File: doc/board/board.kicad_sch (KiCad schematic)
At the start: 11 parts, among them J1 Conn_01x02_Pin, SW2 RotaryEncoder_Switch_MP, U1 CR2013-MI2120, U2 PCM5102A, U3 INA219AxD

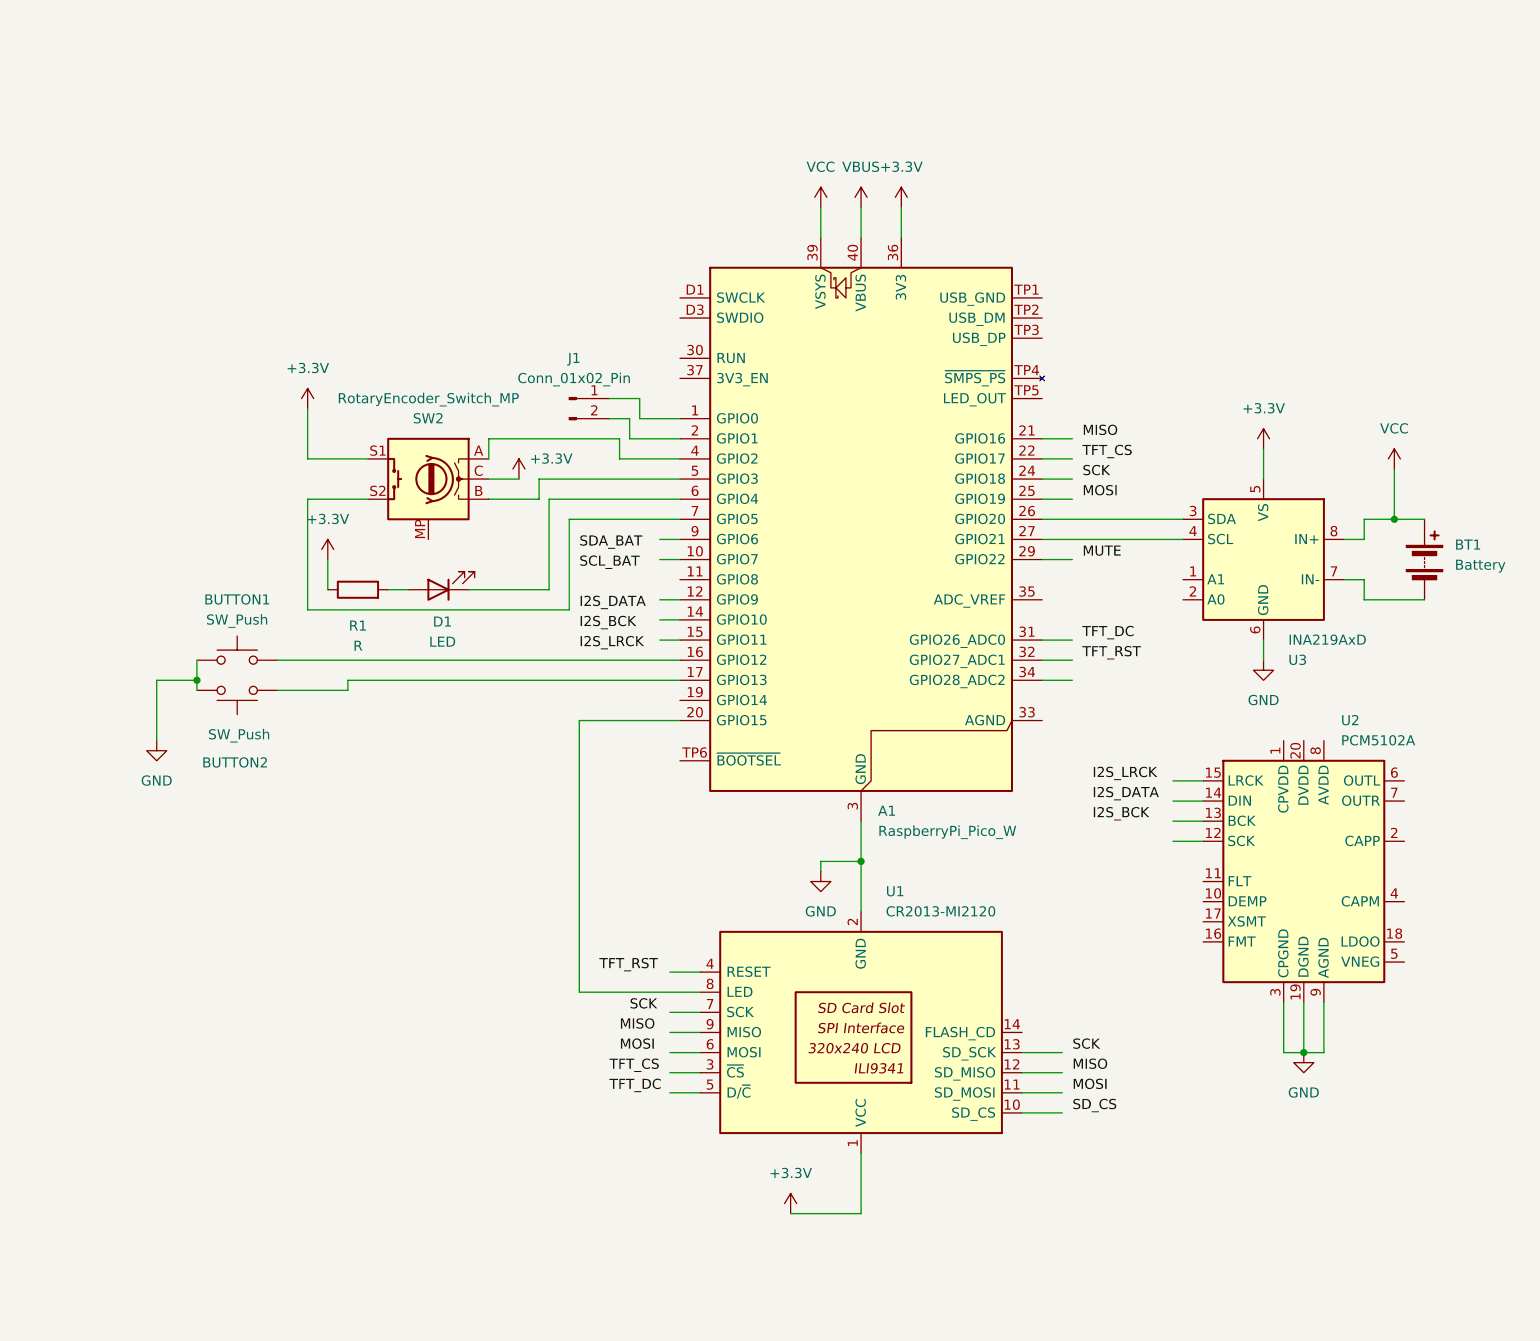
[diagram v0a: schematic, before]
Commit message: doc(datasheets, BoM, schematic)
- Update the schematic with the schmitt trigger
- Add the datasheets for the schmitt trigger
- Add the list of components to reproduce the board
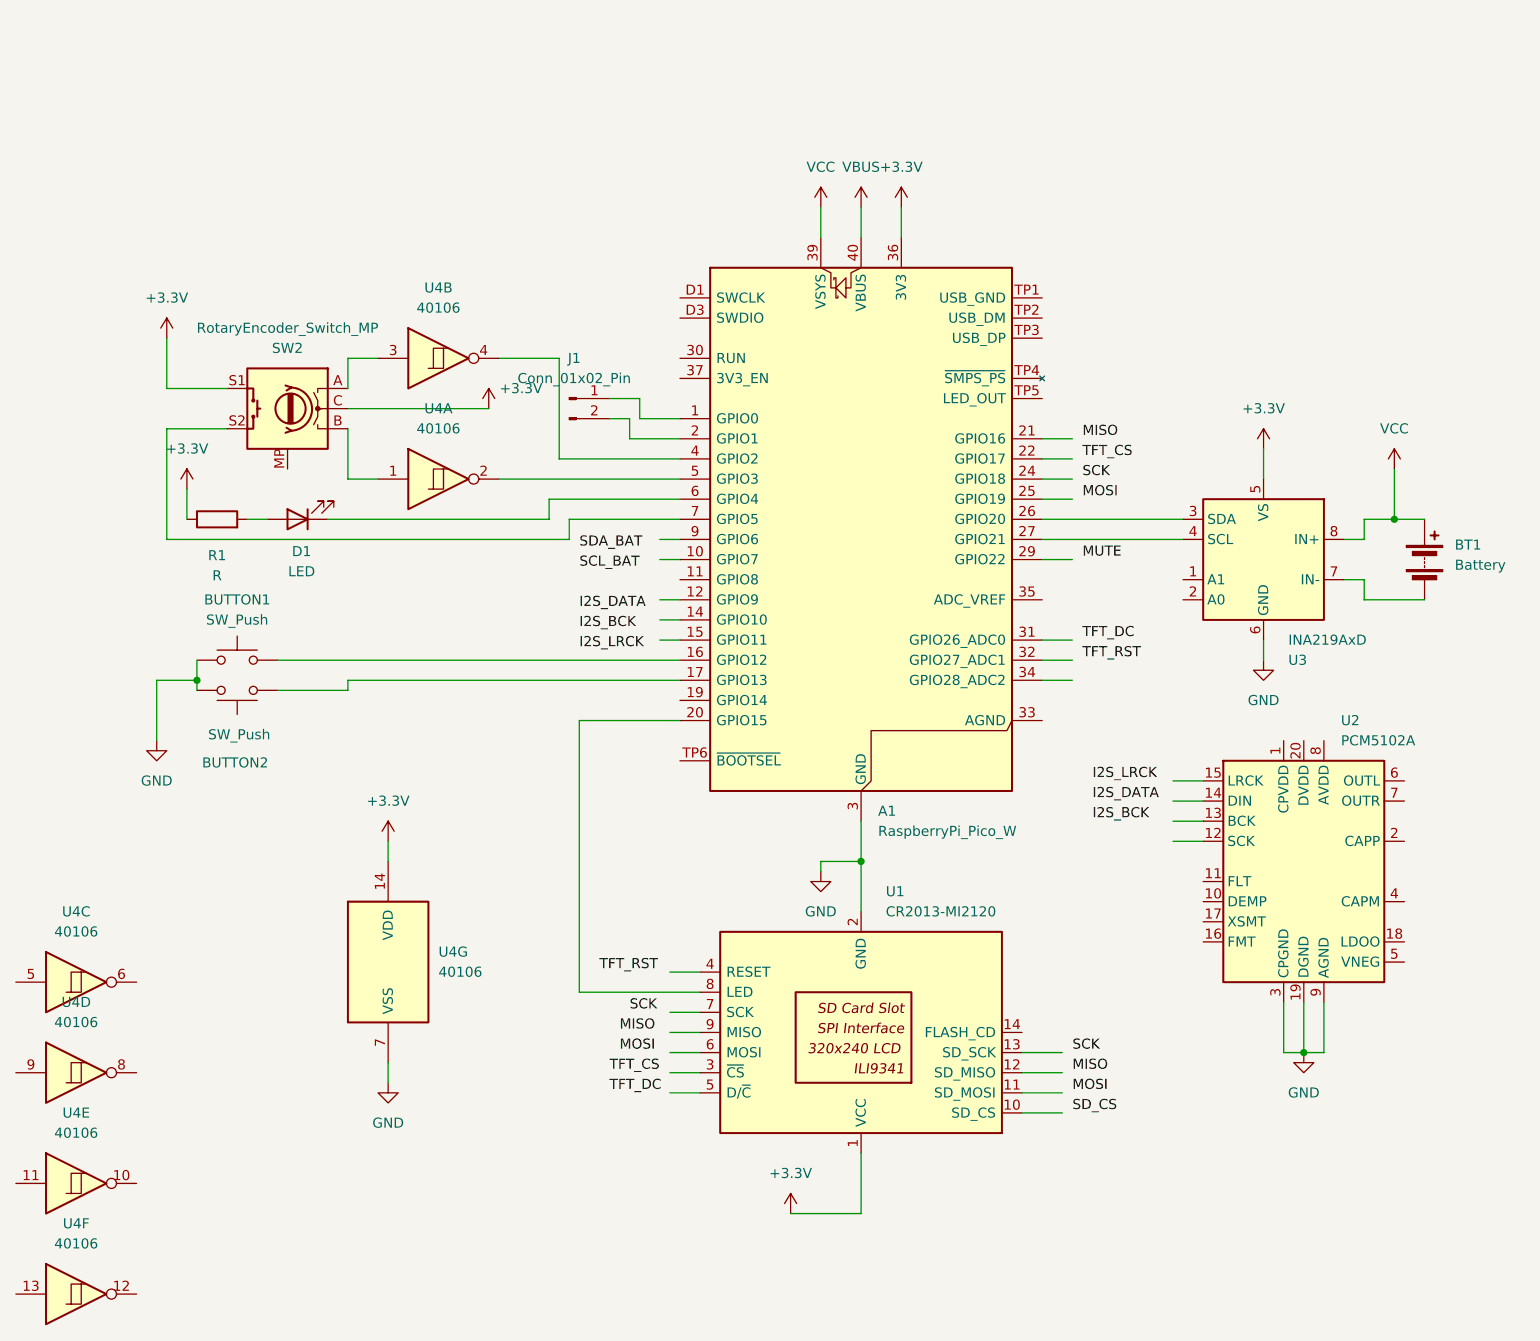
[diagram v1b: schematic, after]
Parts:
- added U4: 40106, symbol 4xxx:40106
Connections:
- net +3.3V: now also U4.14 (VDD)
- net GND: now also U4.7 (VSS)
- net at SW2.A: now also U4.3; no longer A1.4 (GPIO2)
- net at SW2.B: now also U4.1; no longer A1.5 (GPIO3)
- new net: A1.5 (GPIO3), U4.2
- new net: A1.4 (GPIO2), U4.4
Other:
- moved on the sheet: D1, R1, SW2

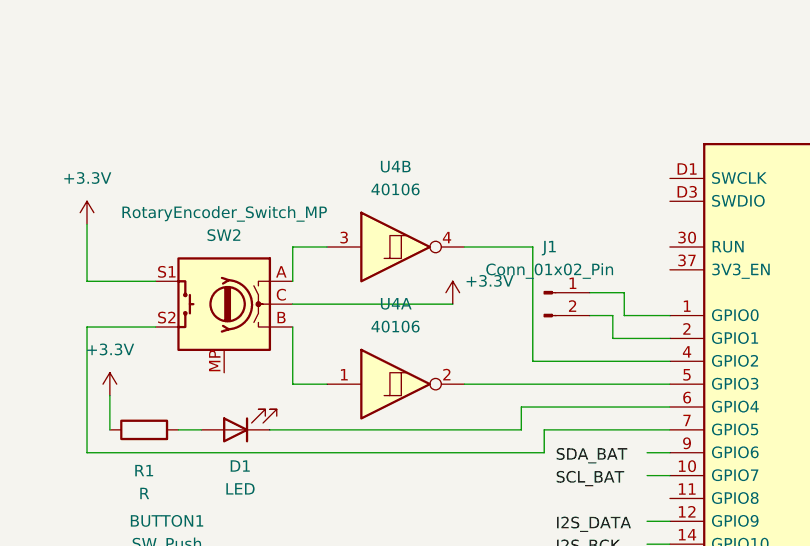
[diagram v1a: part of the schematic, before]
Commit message: feat(encoder): add virtual potentiometer
- Invert encoder input pull direction (from up to down)
- Update schematic to use a schmitt trigger
- Add a virtual potentiometer as feedback to test the encoder
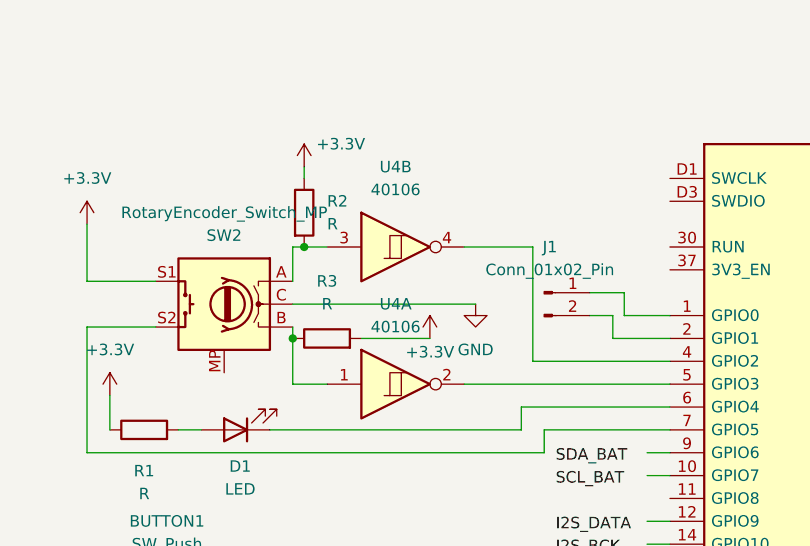
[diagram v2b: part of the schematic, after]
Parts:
- added R2, R3: R, symbol Device:R
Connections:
- net +3.3V: now also R2.1, R3.2; no longer SW2.C
- net GND: now also SW2.C
- net at SW2.A, U4.3: now also R2.2
- net at SW2.B, U4.1: now also R3.1

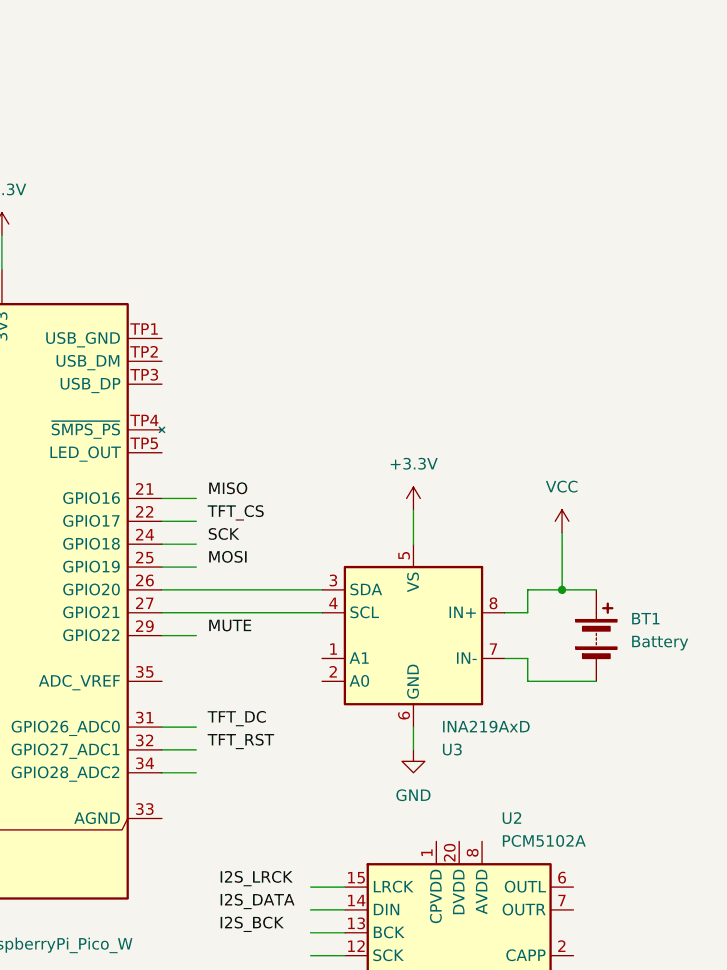
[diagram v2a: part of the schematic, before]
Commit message: doc(schematic): fix I2C assignment in schematic
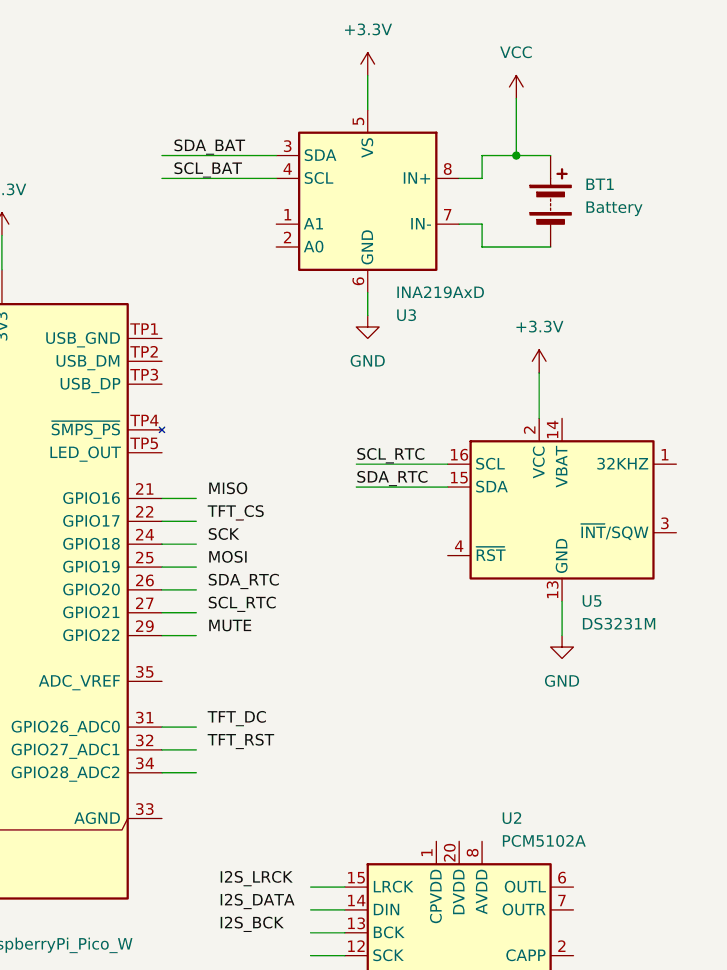
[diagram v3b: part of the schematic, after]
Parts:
- added U5: DS3231M, Package_SO:SOIC-16W_7.5x10.3mm_P1.27mm, symbol Timer_RTC:DS3231M
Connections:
- net +3.3V: now also U5.2 (VCC)
- net GND: now also U5.10 (GND), U5.11 (GND), U5.12 (GND), U5.13 (GND), U5.5 (GND), U5.6 (GND), U5.7 (GND), U5.8 (GND), U5.9 (GND)
- net SCL_BAT: now also U3.4 (SCL)
- net SDA_BAT: now also U3.3 (SDA)
- net at A1.26 (GPIO20): no longer U3.3 (SDA)
- net at A1.27 (GPIO21): no longer U3.4 (SCL)
- new net SCL_RTC: U5.16 (SCL)
- new net SDA_RTC: U5.15 (SDA)
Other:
- moved on the sheet: BT1, U3
